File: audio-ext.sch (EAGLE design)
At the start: 10 parts, among them IC1 LM311N

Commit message: capacitor
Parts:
- added C2: 1u, rcl:C-EUC0805
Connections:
- net +5V: now also C2.1
- net GND: now also C2.2
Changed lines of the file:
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@@
 <part name="C1" library="rcl" library_urn="urn:adsk.eagle:library:334" deviceset="C-EU" device="C0805" package3d_urn="urn:adsk.eagle:package:23617/2"/>
 <part name="AUDIO-IN" library="wirepad" library_urn="urn:adsk.eagle:library:412" deviceset="WIREPAD" device="1,6/0,8" package3d_urn="urn:adsk.eagle:package:30830/1" value=""/>
+<part name="C2" library="rcl" library_urn="urn:adsk.eagle:library:334" deviceset="C-EU" device="C0805" package3d_urn="urn:adsk.eagle:package:23617/2" value="1u"/>
 </parts>
 <sheets>
@@
 <attribute name="VALUE" x="72.263" y="46.482" size="1.778" layer="96" rot="R180"/>
 </instance>
+<instance part="C2" gate="G$1" x="25.4" y="58.42" smashed="yes">
+<attribute name="NAME" x="26.924" y="58.801" size="1.778" layer="95"/>
+<attribute name="VALUE" x="26.924" y="53.721" size="1.778" layer="96"/>
+</instance>
 </instances>
 <busses>
@@
 <pinref part="R2" gate="G$1" pin="2"/>
 <pinref part="P+4" gate="1" pin="+5V"/>
-<wire x1="35.56" y1="78.74" x2="35.56" y2="68.58" width="0.1524" layer="91"/>
+<wire x1="35.56" y1="78.74" x2="35.56" y2="71.12" width="0.1524" layer="91"/>
+<pinref part="C2" gate="G$1" pin="1"/>
+<wire x1="35.56" y1="71.12" x2="35.56" y2="68.58" width="0.1524" layer="91"/>
+<wire x1="25.4" y1="60.96" x2="25.4" y2="71.12" width="0.1524" layer="91"/>
+<wire x1="25.4" y1="71.12" x2="35.56" y2="71.12" width="0.1524" layer="91"/>
+<junction x="35.56" y="71.12"/>
 </segment>
 </net>
@@
 <pinref part="GND1" gate="1" pin="GND"/>
 <wire x1="35.56" y1="40.64" x2="35.56" y2="38.1" width="0.1524" layer="91"/>
+<pinref part="C2" gate="G$1" pin="2"/>
+<wire x1="25.4" y1="53.34" x2="25.4" y2="40.64" width="0.1524" layer="91"/>
+<wire x1="25.4" y1="40.64" x2="35.56" y2="40.64" width="0.1524" layer="91"/>
+<junction x="35.56" y="40.64"/>
 </segment>
 <segment>

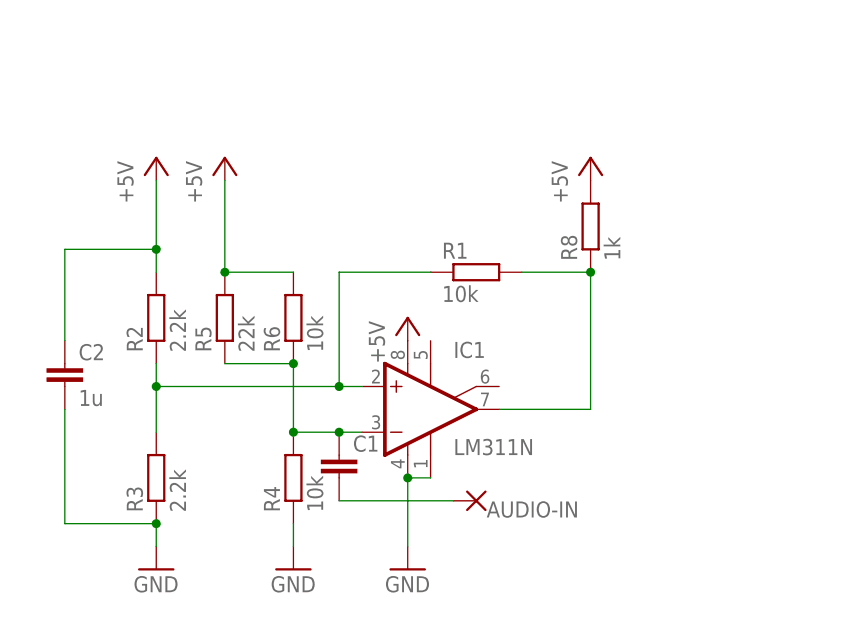
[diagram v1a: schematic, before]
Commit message: overvoltage protect
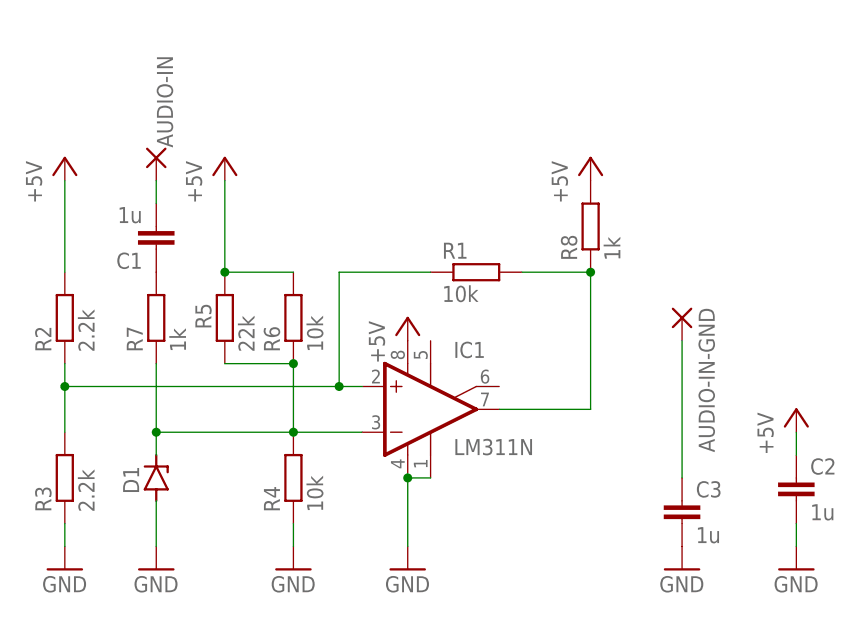
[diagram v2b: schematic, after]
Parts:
- added AUDIO-IN-GND: WIREPAD1,6/0,8, wirepad:WIREPAD1,6/0,8
- added C3: 1u, rcl:C-EUC0805
- added D1: (no value), diode:ZENER-DIODESOT23
- added R7: 1k, rcl:R-EU_R0805
- C1: value (none) -> 1u
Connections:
- new net N$2: AUDIO-IN-GND.P, C3.1
- new net N$6: D1.C, IC1.-IN, R4.2, R5.1, R6.1, R7.1
- net GND: now also C3.2, D1.A
- net N$3: now also R7.2; no longer IC1.-IN, R4.2, R5.1, R6.1
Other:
- moved on the sheet: AUDIO-IN, C1, C2, R2, R3
